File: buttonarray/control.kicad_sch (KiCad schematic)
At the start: 53 parts, among them Q1 2N2219, Q10 2N2219, Q11 2N2219, Q12 2N2219, Q13 2N2219, Q14 2N2219, Q15 2N2219, Q16 2N2219, Q2 2N2219, Q3 2N2219, Q4 2N2219, Q5 2N2219, Q6 2N2219, Q7 2N2219, Q8 2N2219, Q9 2N2219, U1 LM2575-3.3BT

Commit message: add: footprints for button array except switches
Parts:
- C3: footprint (none) -> Capacitor_THT:CP_Radial_D6.3mm_P2.50mm
- C4: footprint (none) -> Capacitor_THT:CP_Radial_D10.0mm_P5.00mm
- L1: footprint (none) -> Inductor_SMD:L_Fastron_PISN_Handsoldering
- R10, R11, R12, R13, R14, R15, R16, R17, R18, R19, R20, R21, R22, R23, R24, R25, R26, R27, R28, R29, R30, R31, R32, R33, R34, R35, R36, R5, R6, R7, R8, R9: footprint (none) -> Resistor_SMD:R_1206_3216Metric_Pad1.30x1.75mm_HandSolder

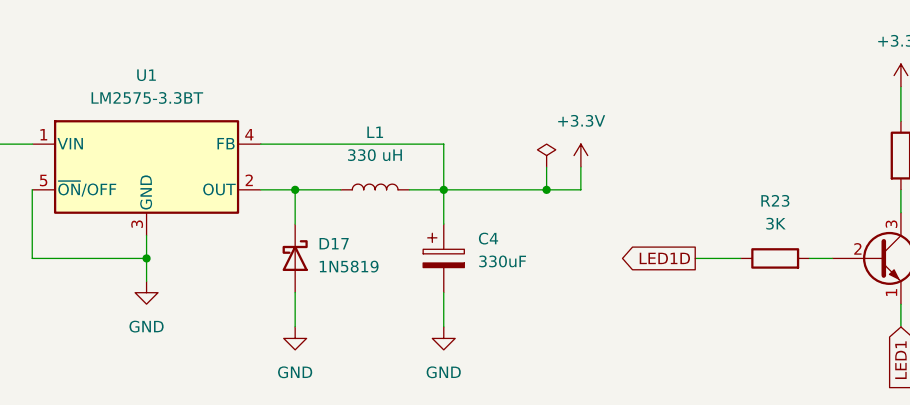
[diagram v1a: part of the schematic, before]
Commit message: add: numpad routing prototype
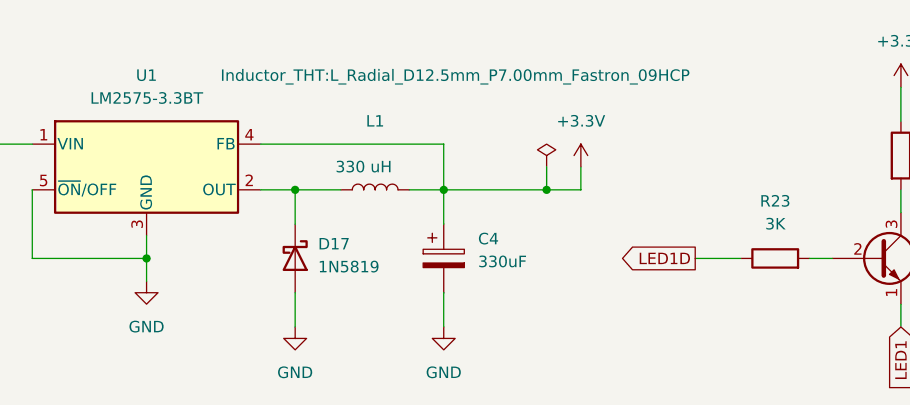
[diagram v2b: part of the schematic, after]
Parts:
- L1: footprint Inductor_SMD:L_Fastron_PISN_Handsoldering -> Inductor_THT:L_Radial_D12.5mm_P7.00mm_Fastron_09HCP
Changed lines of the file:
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@@
   )
   (symbol (lib_id "Device:L") (at 104.14 39.37 90) (unit 1)
-    (in_bom yes) (on_board yes) (fields_autoplaced)
-    (property "Reference" "L1" (id 0) (at 104.14 33.02 90))
-    (property "Value" "330 uH" (id 1) (at 104.14 35.56 90))
-    (property "Footprint" "Inductor_SMD:L_Fastron_PISN_Handsoldering" (id 2) (at 104.14 39.37 0)
-      (effects (font (size 1.27 1.27)) hide)
-    )
+    (in_bom yes) (on_board yes)
+    (property "Reference" "L1" (id 0) (at 104.14 31.75 90))
+    (property "Value" "330 uH" (id 1) (at 102.87 36.83 90))
+    (property "Footprint" "Inductor_THT:L_Radial_D12.5mm_P7.00mm_Fastron_09HCP" (id 2) (at 113.03 26.67 90))
     (property "Datasheet" "~" (id 3) (at 104.14 39.37 0)
       (effects (font (size 1.27 1.27)) hide)
